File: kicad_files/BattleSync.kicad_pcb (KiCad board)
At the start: 2 copper layers, 14 parts, among them SW1 SW_SPDT, U1 ESP32-C3, U2 DFPlayer Mini

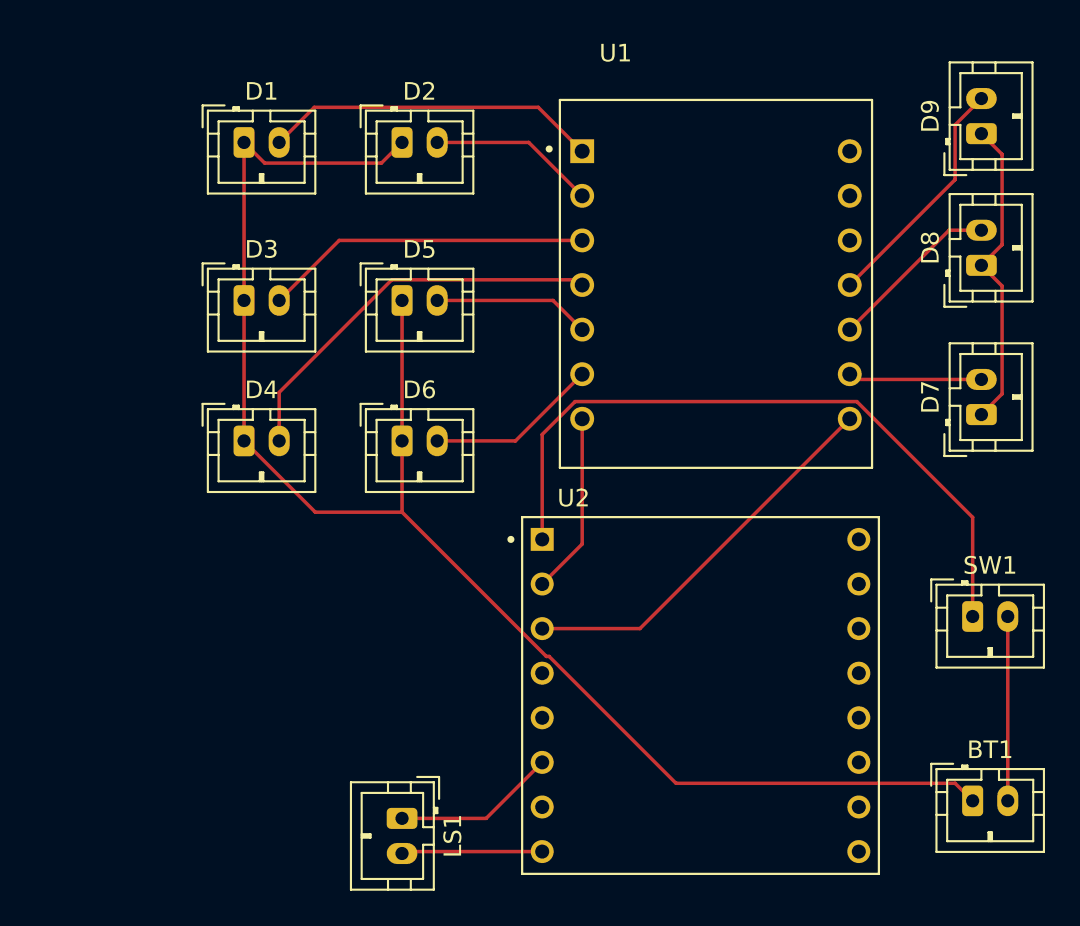
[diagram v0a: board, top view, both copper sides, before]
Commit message: Update PCB design with footprint and net changes
Hardware design updates including:
- Revised net numbering and routing
- Footprint changes (connector and capacitor updates)
- Added Seeeduino XIAO ESP32S3 KiCAD library
- Updated component placement and connections

These changes align the PCB design with the ESP32-S3 hardware migration.

🤖 Generated with [Claude Code](https://claude.com/claude-code)

Co-Authored-By: Claude <noreply@anthropic.com>
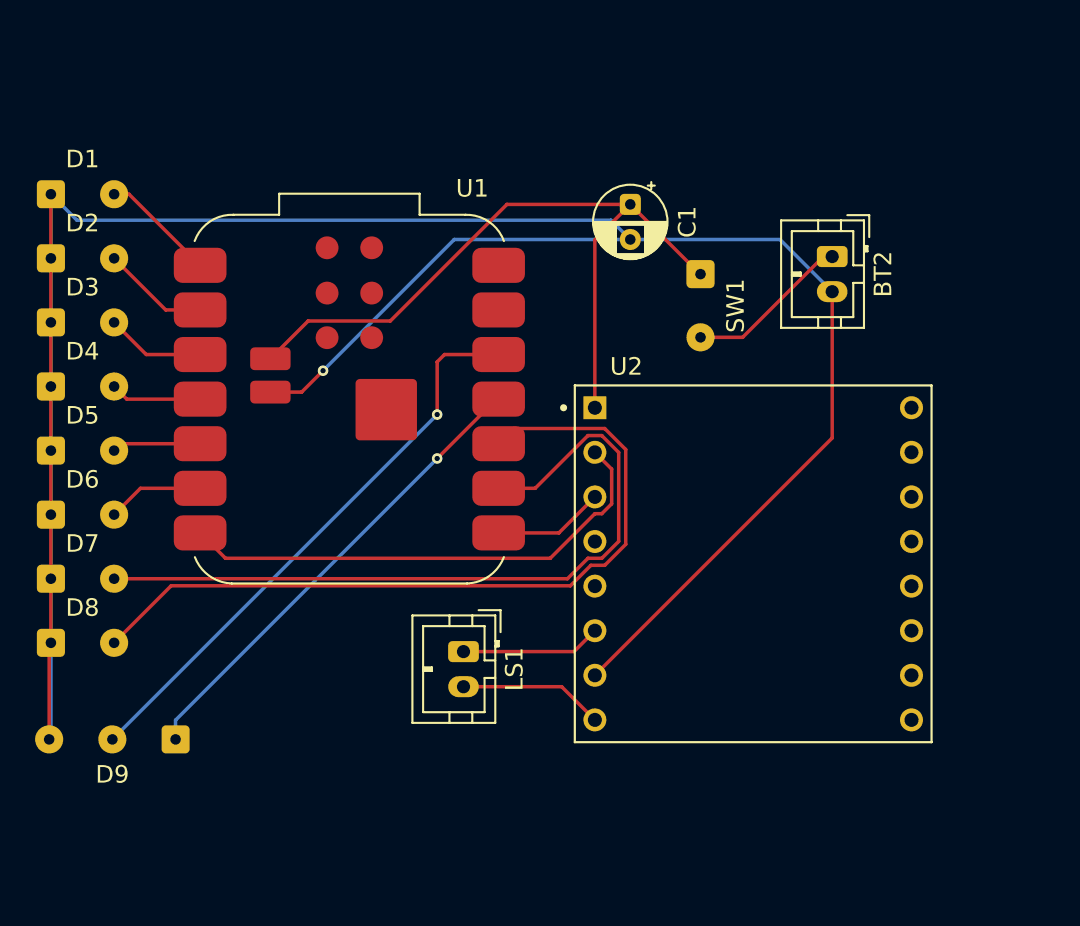
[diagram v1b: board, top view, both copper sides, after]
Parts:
- removed BT1: Battery_Cell, Connector_JST:JST_PH_B2B-PH-K_1x02_P2.00mm_Vertical
- added BT2: Battery_Cell, Connector_JST:JST_PH_B2B-PH-K_1x02_P2.00mm_Vertical, F.Cu at (76.5, 26.0)
- added C1: C_Polarized, Capacitor_THT:CP_Radial_D4.0mm_P2.00mm, F.Cu at (65.0, 23.0)
- D1, D2, D3, D4, D5, D6, D7, D8, SW1: footprint Connector_JST:JST_PH_B2B-PH-K_1x02_P2.00mm_Vertical -> Connector_Wire:SolderWire-0.1sqmm_1x02_P3.6mm_D0.4mm_OD1mm
- D9: footprint Connector_JST:JST_PH_B2B-PH-K_1x02_P2.00mm_Vertical -> Connector_Wire:SolderWire-0.1sqmm_1x03_P3.6mm_D0.4mm_OD1mm
- U1: value ESP32-C3 -> ESP32-S3; footprint Seeeduino xiao ESP32C3 KiCAD Library:MODULE_113991054 -> RF_Module:MCU_Seeed_ESP32C3
- U2: value DFPlayer Mini -> DFR0299
- moved D9 57.4 mm to (39.1, 53.5), turned to 180 degrees
- moved D8 57.2 mm to (32.0, 48.0), turned to 0 degrees
- moved D7 53.8 mm to (32.0, 44.4), turned to 0 degrees
- moved SW1 24.9 mm to (69.0, 27.0), turned to -90 degrees
- moved U1 21.9 mm to (49.0, 34.1)
- moved D5 21.8 mm to (32.0, 37.0)
- moved D2 21.1 mm to (32.0, 26.1)
- moved D6 20.4 mm to (32.0, 40.7)
- moved D4 11.4 mm to (32.0, 33.4)
- moved D1 11.4 mm to (32.0, 22.4)
- moved D3 11.1 mm to (32.0, 29.8)
- moved LS1 10.1 mm to (55.5, 48.5)
- moved U2 8.08 mm to (72.0, 43.5)
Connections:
- D1 pad 1: Net-(BT1-+) -> Net-(BT2--)
- D2 pad 1: Net-(BT1-+) -> Net-(BT2--)
- D3 pad 1: Net-(BT1-+) -> Net-(BT2--)
- D4 pad 1: Net-(BT1-+) -> Net-(BT2--)
- D5 pad 1: Net-(BT1-+) -> Net-(BT2--)
- D6 pad 1: Net-(BT1-+) -> Net-(BT2--)
- D7 pad 1: Net-(BT1-+) -> Net-(BT2--)
- D8 pad 1: Net-(BT1-+) -> Net-(BT2--)
- D9 pad 1: Net-(BT1-+) -> Net-(D9-VDD)
- U1 pad 11: Net-(D9-A) -> Net-(D9-DIN)
- U1 pad 12: unconnected-(U1-3V3-Pad12) -> Net-(D9-VDD)
- U2 pad 7: Net-(BT1-+) -> Net-(BT2--)
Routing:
- net Net-(BT2--): track 0.00 -> 160.5 mm, vias 0 -> 1
- net Net-(BT1-+): track 107.0 -> 0.00 mm
- net Net-(D7-A): track 7.62 -> 43.2 mm
- net Net-(D8-A): track 9.84 -> 45.0 mm
- net Net-(D9-VDD): track 0.00 -> 32.8 mm, vias 0 -> 1
- net Net-(D9-DIN): track 0.00 -> 27.1 mm, vias 0 -> 1
- net Net-(U1-GPIO21_D6_TX): track 10.4 -> 28.7 mm
- net Net-(D4-A): track 22.8 -> 5.20 mm
- net Net-(U1-GPIO20_D7_RX): track 22.5 -> 6.33 mm
- net Net-(D9-A): track 13.7 -> 0.00 mm
- net Net-(D3-A): track 18.7 -> 5.66 mm
- net Net-(D1-A): track 19.1 -> 6.58 mm
- net Net-(D6-A): track 9.83 -> 5.52 mm
- net Net-(D5-A): track 8.95 -> 5.06 mm
- net Net-(D2-A): track 9.52 -> 6.12 mm
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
